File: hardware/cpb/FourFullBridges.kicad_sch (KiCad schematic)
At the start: 32 parts, among them Q5 PMBT2222A, Q6 IRF9393, Q7 PMBT2222A, U7 SC18IS606, U8 KF33BDT, U9 MAX22200

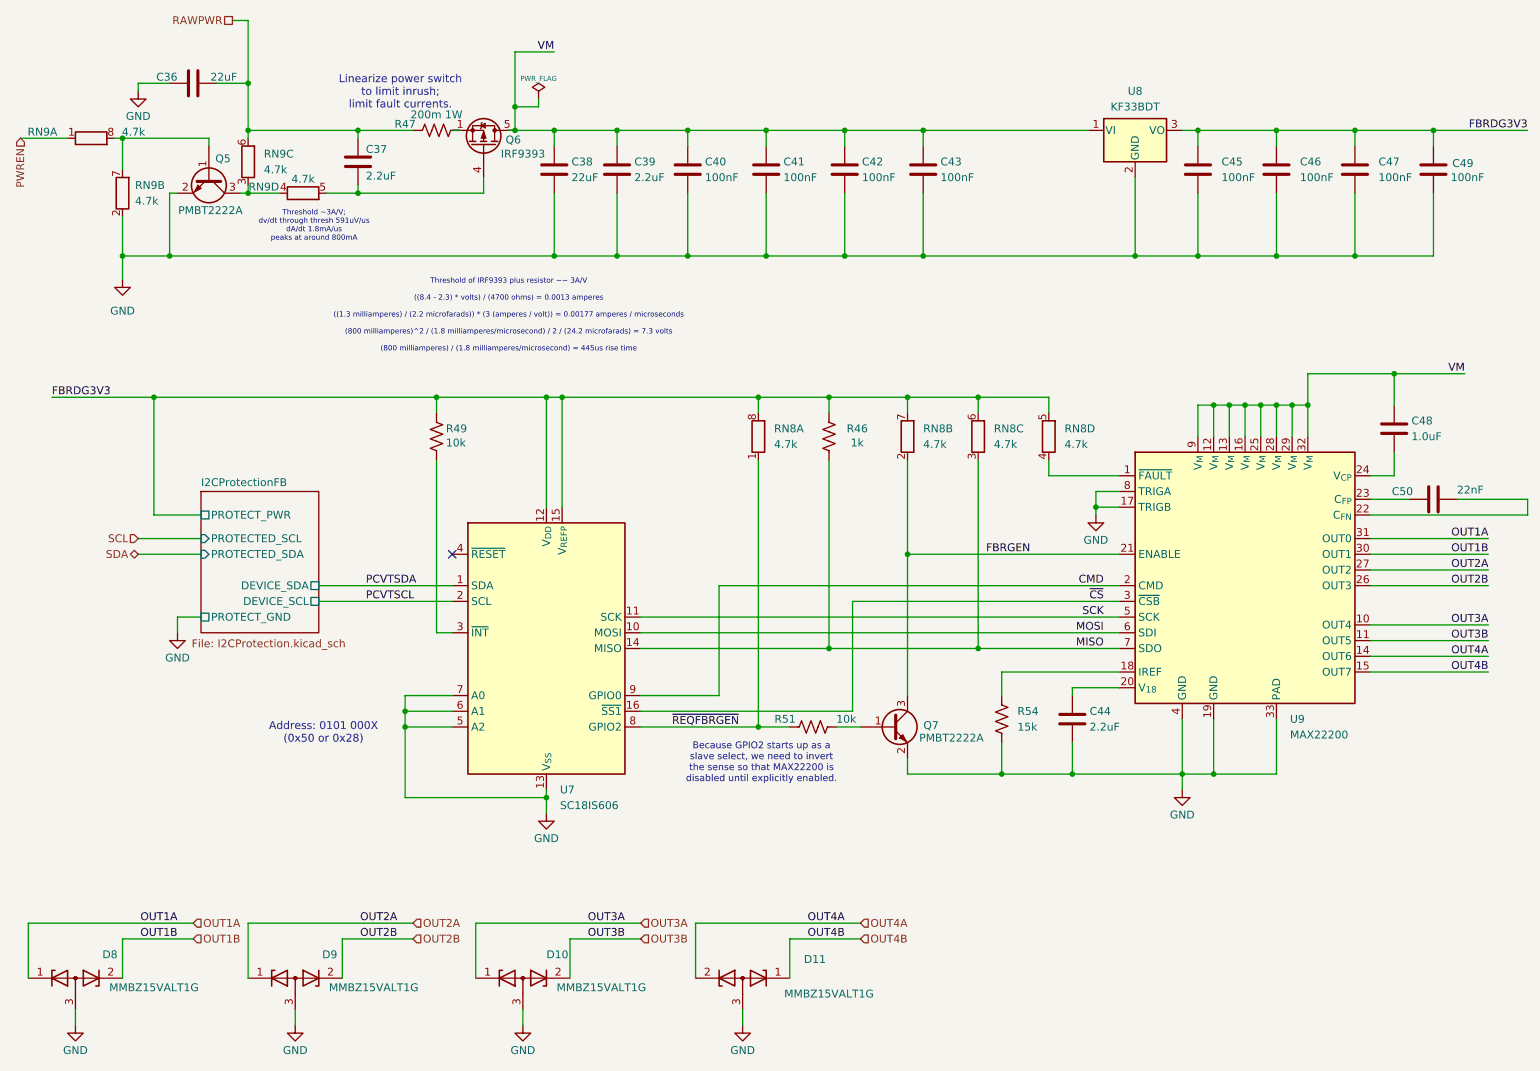
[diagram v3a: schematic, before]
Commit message: hardware/cpb: finished revisions
did all things specified on Errata file for cpb;
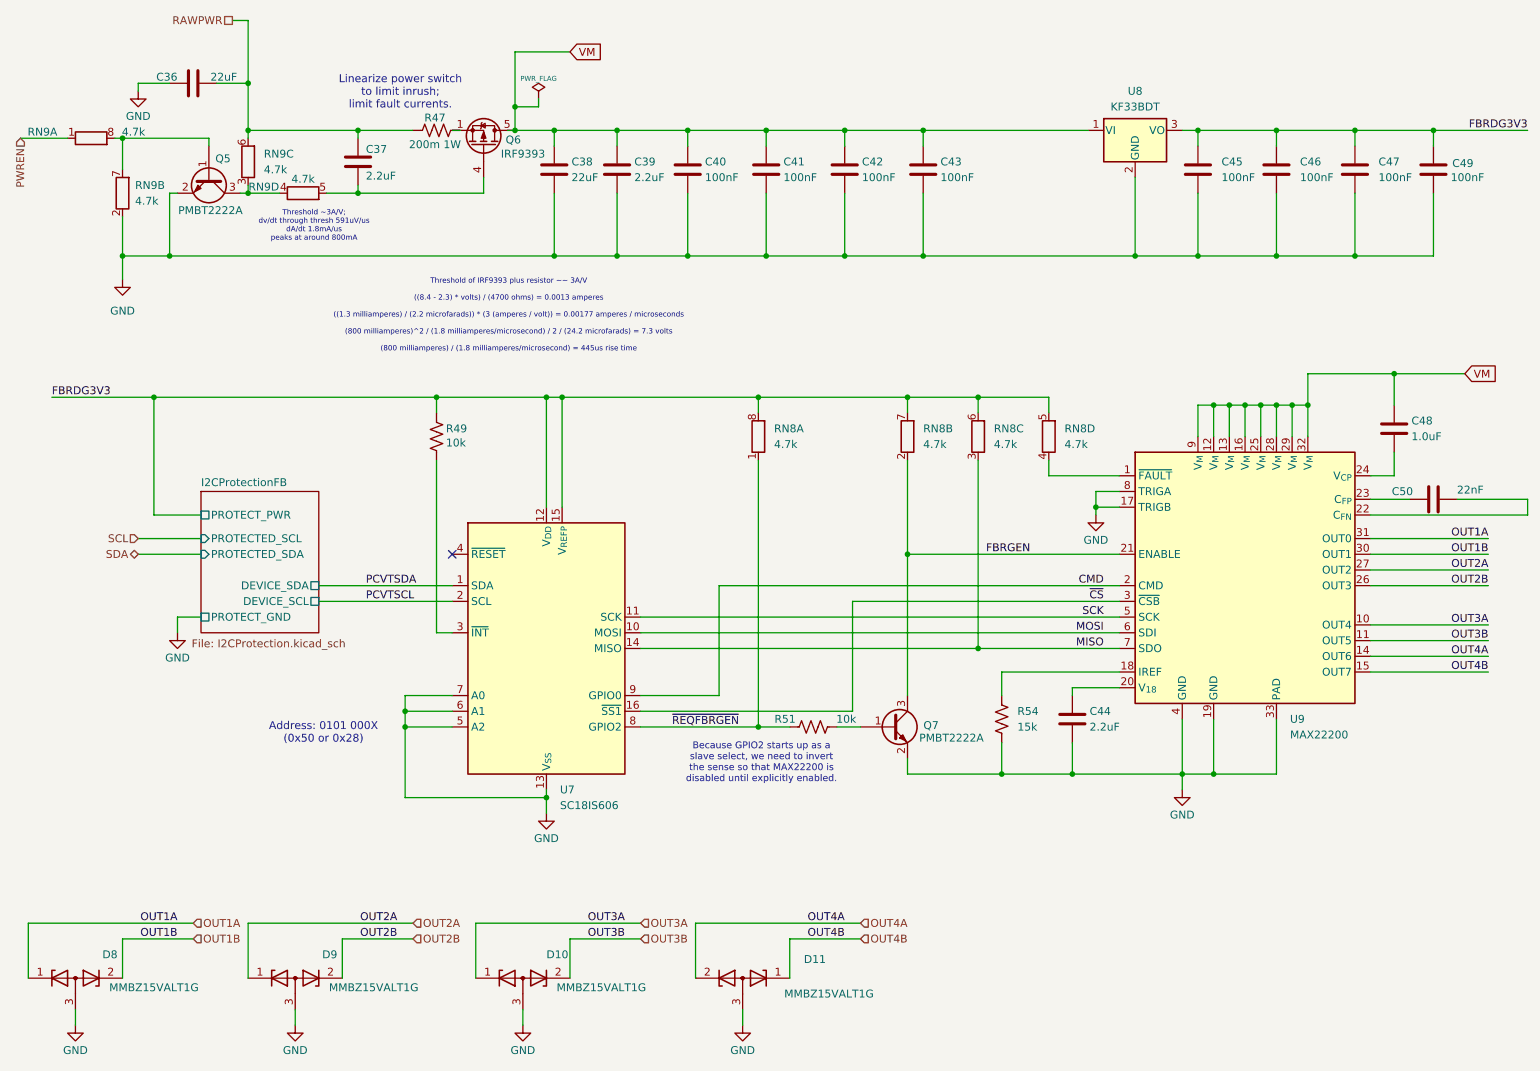
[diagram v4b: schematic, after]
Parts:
- removed R46: 1k, Resistor_SMD:R_0603_1608Metric, symbol Device:R_US
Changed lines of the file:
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@@
 	)
 	(junction
-		(at 144.78 93.98)
-		(diameter 0)
-		(color 0 0 0 0)
-	)
-	(junction
 		(at 99.06 93.98)
 		(diameter 0)
@@
 	)
 	(junction
-		(at 144.78 134.62)
-		(diameter 0)
-		(color 0 0 0 0)
-	)
-	(junction
 		(at 147.32 71.12)
 		(diameter 0)
@@
 	(wire
 		(pts
-			(xy 114.3 134.62) (xy 144.78 134.62)
+			(xy 114.3 134.62) (xy 168.91 134.62)
 		)
 		(stroke
@@
 	(wire
 		(pts
-			(xy 144.78 93.98) (xy 157.48 93.98)
-		)
-		(stroke
-			(width 0)
-			(type default)
-		)
-	)
-	(wire
-		(pts
 			(xy 38.1 71.12) (xy 100.33 71.12)
 		)
@@
 	(wire
 		(pts
-			(xy 144.78 93.98) (xy 144.78 96.52)
-		)
-		(stroke
-			(width 0)
-			(type default)
-		)
-	)
-	(wire
-		(pts
 			(xy 45.72 43.18) (xy 50.8 43.18)
 		)
@@
 	(wire
 		(pts
-			(xy 144.78 134.62) (xy 168.91 134.62)
-		)
-		(stroke
-			(width 0)
-			(type default)
-		)
-	)
-	(wire
-		(pts
 			(xy 204.47 71.12) (xy 194.31 71.12)
 		)
@@
 	(wire
 		(pts
-			(xy 93.98 38.1) (xy 100.33 38.1)
+			(xy 93.98 38.1) (xy 102.87 38.1)
 		)
 		(stroke
@@
 	(wire
 		(pts
-			(xy 144.78 104.14) (xy 144.78 134.62)
-		)
-		(stroke
-			(width 0)
-			(type default)
-		)
-	)
-	(wire
-		(pts
 			(xy 236.22 90.17) (xy 236.22 95.25)
 		)
@@
 	(wire
 		(pts
-			(xy 133.35 93.98) (xy 144.78 93.98)
+			(xy 133.35 93.98) (xy 157.48 93.98)
 		)
 		(stroke
@@
 		)
 	)
-	(label "VM"
-		(at 247.65 90.17 180)
-		(fields_autoplaced yes)
-		(effects
-			(font
-				(size 1.27 1.27)
-			)
-			(justify right bottom)
-		)
-	)
 	(label "FBRGEN"
 		(at 170.18 119.38 0)
@@
 		)
 	)
-	(label "VM"
-		(at 100.33 38.1 180)
-		(fields_autoplaced yes)
-		(effects
-			(font
-				(size 1.27 1.27)
-			)
-			(justify right bottom)
-		)
-	)
 	(label "MOSI"
 		(at 189.23 132.08 180)
@@
 		)
 	)
+	(global_label "VM"
+		(shape input)
+		(at 102.87 38.1 0)
+		(fields_autoplaced yes)
+		(effects
+			(font
+				(size 1.27 1.27)
+			)
+			(justify left)
+		)
+		(property "Intersheetrefs" "${INTERSHEET_REFS}"
+			(at 108.3952 38.1 0)
+			(effects
+				(font
+					(size 1.27 1.27)
+				)
+				(justify left)
+				(hide yes)
+			)
+		)
+	)
+	(global_label "VM"
+		(shape input)
+		(at 247.65 90.17 0)
+		(fields_autoplaced yes)
+		(effects
+			(font
+				(size 1.27 1.27)
+			)
+			(justify left)
+		)
+		(property "Intersheetrefs" "${INTERSHEET_REFS}"
+			(at 253.1752 90.17 0)
+			(effects
+				(font
+					(size 1.27 1.27)
+				)
+				(justify left)
+				(hide yes)
+			)
+		)
+	)
 	(hierarchical_label "OUT2B"
 		(shape input)
@@
 	)
 	(symbol
-		(lib_id "Device:R_US")
-		(at 144.78 100.33 180)
-		(unit 1)
-		(exclude_from_sim no)
-		(in_bom yes)
-		(on_board yes)
-		(dnp no)
-		(property "Reference" "R46"
-			(at 149.352 99.06 0)
-			(effects
-				(font
-					(size 1.27 1.27)
-				)
-			)
-		)
-		(property "Value" "1k"
-			(at 149.352 101.346 0)
-			(effects
-				(font
-					(size 1.27 1.27)
-				)
-			)
-		)
-		(property "Footprint" "Resistor_SMD:R_0603_1608Metric"
-			(at 146.558 100.33 90)
-			(effects
-				(font
-					(size 1.27 1.27)
-				)
-				(hide yes)
-			)
-		)
-		(property "Datasheet" "~"
-			(at 144.78 100.33 0)
-			(effects
-				(font
-					(size 1.27 1.27)
-				)
-				(hide yes)
-			)
-		)
-		(property "Description" "Resistor"
-			(at 144.78 100.33 0)
-			(effects
-				(font
-					(size 1.27 1.27)
-				)
-				(hide yes)
-			)
-		)
-		(property "LCSC" "C22548"
-			(at 144.78 100.33 0)
-			(effects
-				(font
-					(size 1.27 1.27)
-				)
-				(hide yes)
-			)
-		)
-		(pin "2"
-		)
-		(pin "1"
-		)
-		(instances
-			(project "cpb"
-				(path "/9a10a1ee-db5a-47ad-90f3-81b92d74d449/1d0e9b27-ccf6-43da-9db7-61f18e9cbbee"
-					(reference "R46")
-					(unit 1)
-				)
-			)
-		)
-	)
-	(symbol
 		(lib_id "power:GND")
 		(at 95.25 195.58 0)
@@
 		(dnp no)
 		(property "Reference" "R47"
-			(at 76.2 49.784 90)
+			(at 81.026 48.768 90)
 			(effects
 				(font
@@
 		)
 		(property "Value" "200m 1W"
-			(at 81.28 48.26 90)
+			(at 81.026 53.086 90)
 			(effects
 				(font

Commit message: hardware/cpb: changed labels, spread out components
changed vm labels, spread out somponents on Four Full Bridges sch;
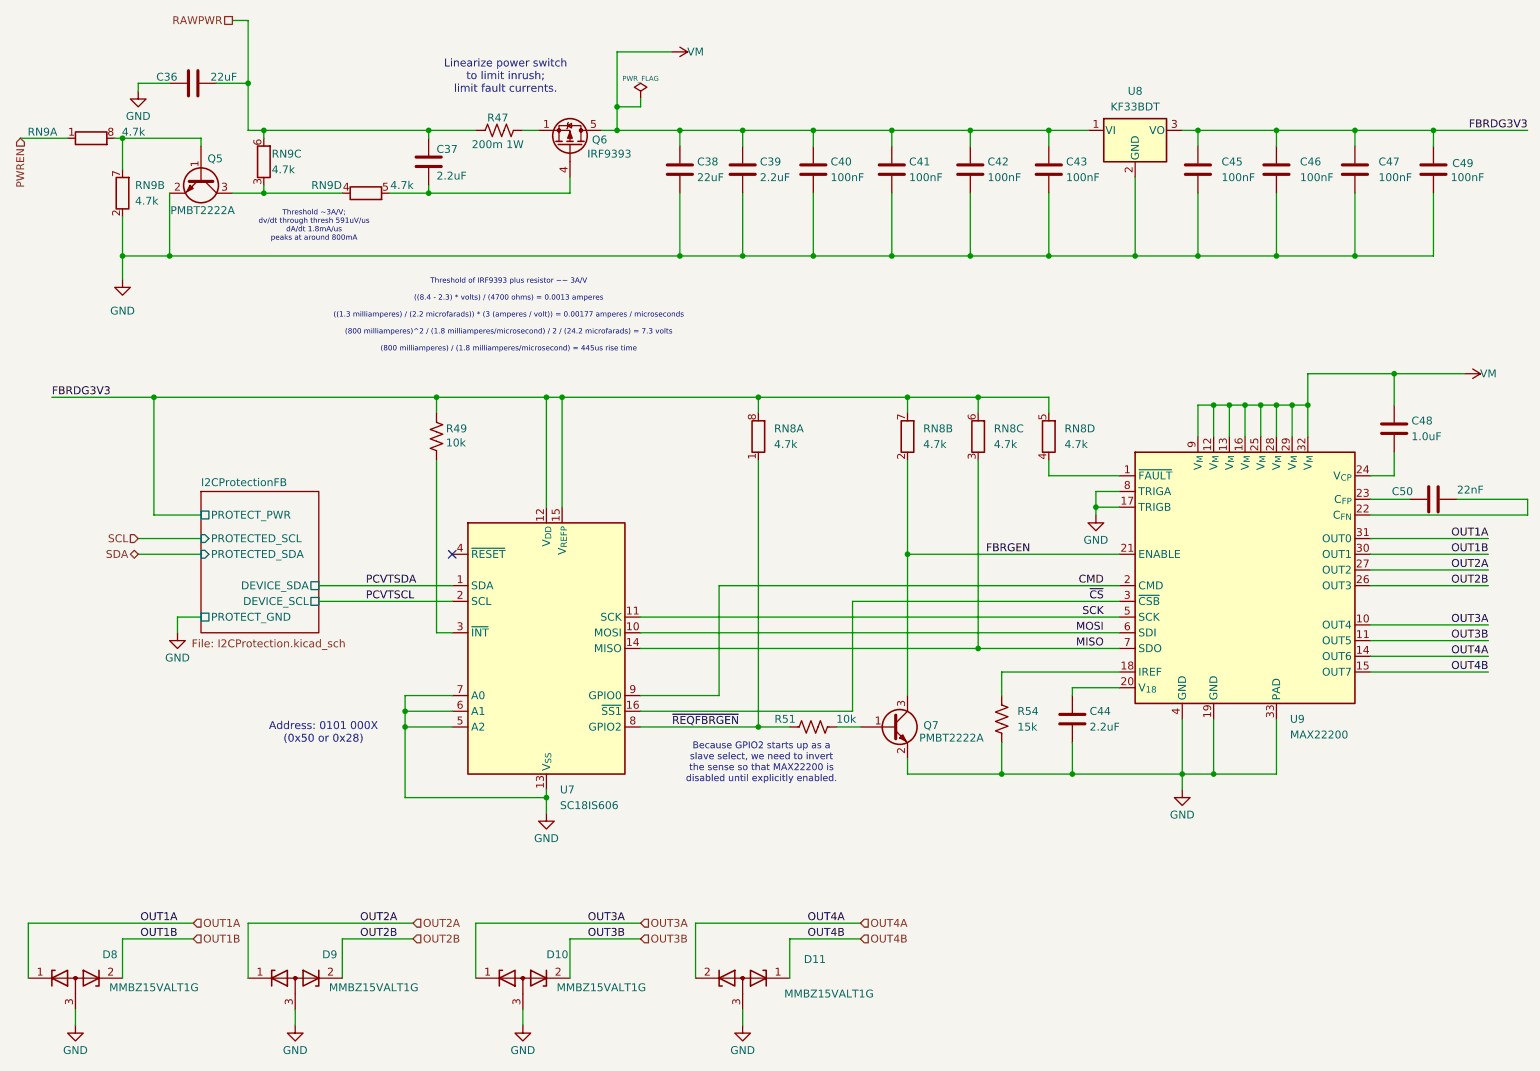
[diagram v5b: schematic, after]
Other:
- moved on the sheet: C37, C38, C39, C40, C41, C42, C43, Q5, Q6, R47, RN9C, RN9D
